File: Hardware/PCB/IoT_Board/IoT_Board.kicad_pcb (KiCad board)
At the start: 2 copper layers, 100 x 50 mm, 109 parts, among them IC1 VS1838B, IC2 TPS563200DDCR, J10 Conn_01x02_Pin, J14 MAX_98357, J15 INMP_441, J2 Debug UART0, J4 UART1, J5 I2C, J6 CT1, J7 CT2, J9 USB_C_Receptacle_USB2.0_16P, K1 Relay_SPDT, K2 Relay_SPDT, Q1 AO3400A, Q2 AO3400A, Q3 AO3400A, SW1 SW_Push, SW2 SW_Push, SW3 SW_Push, SW4 SW_Push, U1 ESP32-S3-WROOM-1, U2 ME6211C50M5, U5 PC817, U6 PC817

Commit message: Final
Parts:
- renumbered J10 to 5V1, J6 to CT1, J7 to CT2, J5 to I2C1, J15 to INMP_441, D8 to LED_RL1, D9 to LED_RL2, J14 to MAX_98357, J2 to UART0, J4 to UART1
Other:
- board text added: "."

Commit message: add gerber OK
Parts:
- renumbered SW2 to BOOT1, SW3 to BUT1, SW4 to BUT2, SW1 to EN1
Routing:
- net +3V3: track 116.9 -> 112.8 mm, vias 28 -> 25
- net GND: track 116.9 -> 121.0 mm

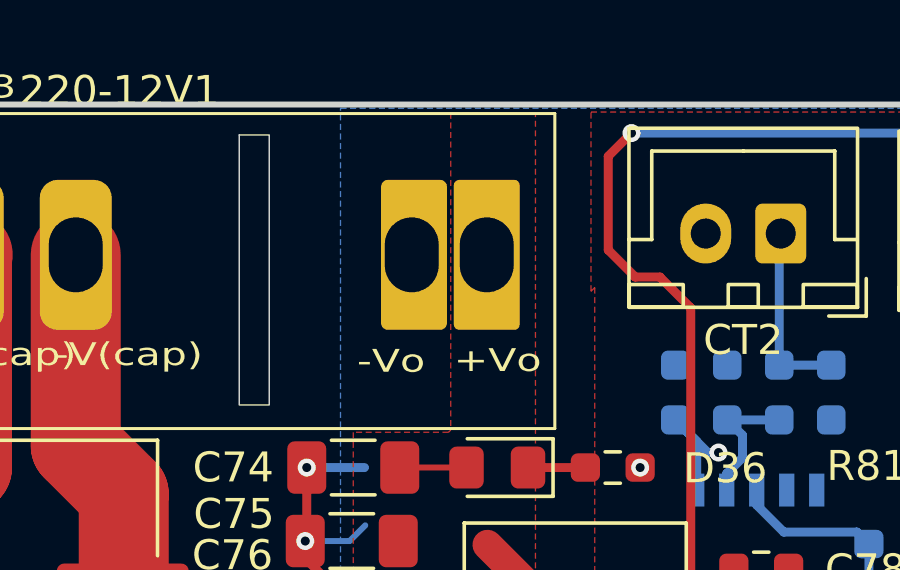
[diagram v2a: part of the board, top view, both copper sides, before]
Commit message: feat: Add Smart Home Gateway (Sherpa-ONNX, Qwen LLM, EdgeTTS, Closed-Loop Verifier), Master Plan & update PCB design
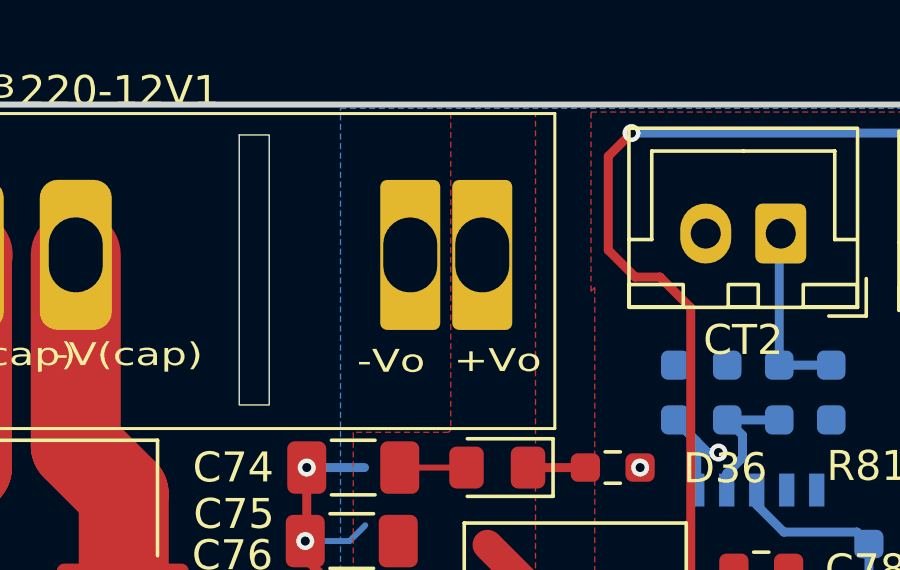
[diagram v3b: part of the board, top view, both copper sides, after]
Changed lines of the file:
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@@
 		(sheetname "/")
 		(sheetfile "IoT_Board.kicad_sch")
-		(units
-			(unit
-				(name "A")
-				(pins "1" "2" "3" "4" "6" "5")
-			)
-		)
 		(duplicate_pad_numbers_are_jumpers no)
 		(fp_line
@@
 		)
 		(pad "5" thru_hole roundrect
-			(at 9.75 -0.00354 90)
-			(size 5 2.2)
-			(drill oval 2.5 1.8
-				(offset -0.000011 0.0752)
-			)
+			(at 9.7 0 90)
+			(size 5 2)
+			(drill oval 2.5 1.8)
 			(layers "*.Cu" "*.Mask")
 			(remove_unused_layers no)
-			(roundrect_rratio 0.1041666667)
+			(roundrect_rratio 0.1136363636)
 			(net "GND")
 			(pinfunction "-Vo_5")
@@
 		)
 		(pad "6" thru_hole roundrect
-			(at 12.25 -0.00354 90)
-			(size 5 2.2)
+			(at 12.1 0 90)
+			(size 5 2)
 			(drill oval 2.5 1.8)
 			(layers "*.Cu" "*.Mask")
 			(remove_unused_layers no)
-			(roundrect_rratio 0.08333333333)
+			(roundrect_rratio 0.1136363636)
 			(net "+12V")
 			(pinfunction "+Vo_6")
@@
 		(model "D:/Home-Assistant-IoT-/Hardware/PCB/lIB/3D/LS05-23BxxDR3.stp"
 			(offset
-				(xyz 0.15 -0.5 9.5)
+				(xyz 0.005 -0.5 9.5)
 			)
 			(scale
@@
 		(target_delay_max 1000000)
 		(target_delay_min 0)
-		(target_length 8.264)
+		(target_length 8.263999)
 		(target_length_max 8.364)
 		(target_length_min 8.164)

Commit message: fix nhieu bug
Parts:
- removed C3: 10uF, Capacitor_SMD:CP_Elec_10x10.5
